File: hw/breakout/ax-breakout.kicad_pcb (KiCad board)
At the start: 2 copper layers, 19 x 16 mm, 28 parts, among them IC1 TG-5006CJ, IC2 AX5243, IC3 RFM22

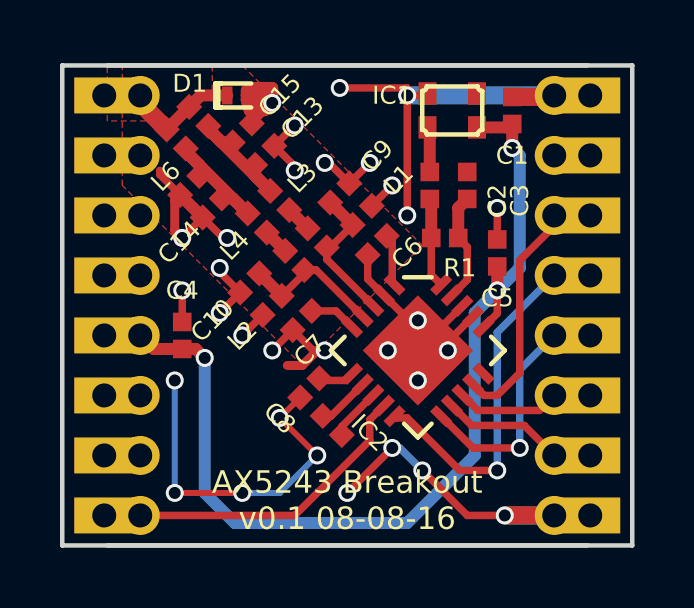
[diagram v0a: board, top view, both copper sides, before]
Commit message: [hw] tidy boms, regen artifacts, update READMEs
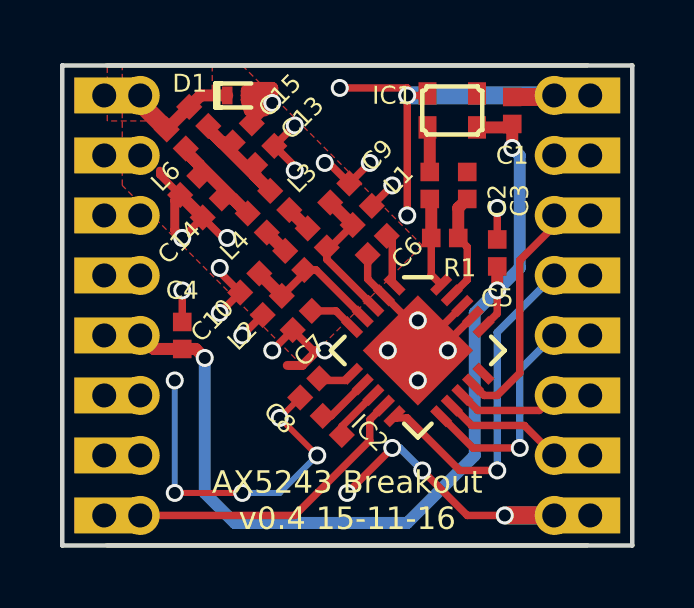
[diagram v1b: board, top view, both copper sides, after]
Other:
- board text added: "AX5243 Breakout v0.4 15-11-16"
- board text removed: "AX5243 Breakout v0.1 08-08-16"
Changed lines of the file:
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@@
     (links 81)
     (no_connects 0)
-    (area 152.924999 100.924999 172.075001 117.075001)
+    (area 146.592858 95.8 172.100001 120.235)
     (thickness 1)
     (drawings 39)
@@
     (34 B.Paste user)
     (35 F.Paste user)
-    (36 B.SilkS user hide)
-    (37 F.SilkS user hide)
+    (36 B.SilkS user)
+    (37 F.SilkS user)
     (38 B.Mask user)
     (39 F.Mask user)
@@
   )
   (setup
-    (last_trace_width 0.2)
+    (last_trace_width 0.25)
     (user_trace_width 0.1524)
     (user_trace_width 0.2)
@@
     (effects (font (size 0.8 0.8) (thickness 0.125)) (justify mirror))
   )
-  (gr_text "AX5243 Breakout\nv0.1 08-08-16" (at 162.5 115.5) (layer F.SilkS)
+  (gr_text "AX5243 Breakout\nv0.4 15-11-16" (at 162.5 115.5) (layer F.SilkS)
     (effects (font (size 0.75 0.75) (thickness 0.12)))
   )
@@
   (segment (start 160.25 115.25) (end 159 115.25) (width 0.2) (layer B.Cu) (net 2))
   (via (at 159 115.25) (size 0.6) (drill 0.4) (layers F.Cu B.Cu) (net 2))
-  (segment (start 160.931802 112.068198) (end 160.25 112.75) (width 0.2) (layer F.Cu) (net 2) (status 400000))
+  (segment (start 160.931802 112.068198) (end 160.25 112.75) (width 0.2) (layer F.Cu) (net 2))
   (via (at 160.25 112.75) (size 0.6) (drill 0.4) (layers F.Cu B.Cu) (net 2))
   (segment (start 160.25 112.75) (end 161.5 114) (width 0.2) (layer F.Cu) (net 2))
